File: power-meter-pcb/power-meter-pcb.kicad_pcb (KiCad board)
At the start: 2 copper layers, 0.7 x 0.5 mm, 59 parts, among them J1 Crank interconnect, J2 Debug, J3 USB4120-03-C_REVA, J4 Side A, J5 Side B, Q1 AS2302, Q2 AS2302, Q3 AS2302, SW1 EN, SW2 BOOT, U1 ESP32-S3-WROOM-1, U2 P3T1755, U3 MCP73831-2-OT, U4 TPD3E001DRLR, U5 S-8261AAJMD-G2JT2U, U6 TPS63031DSK, U7 ADS1232IPW

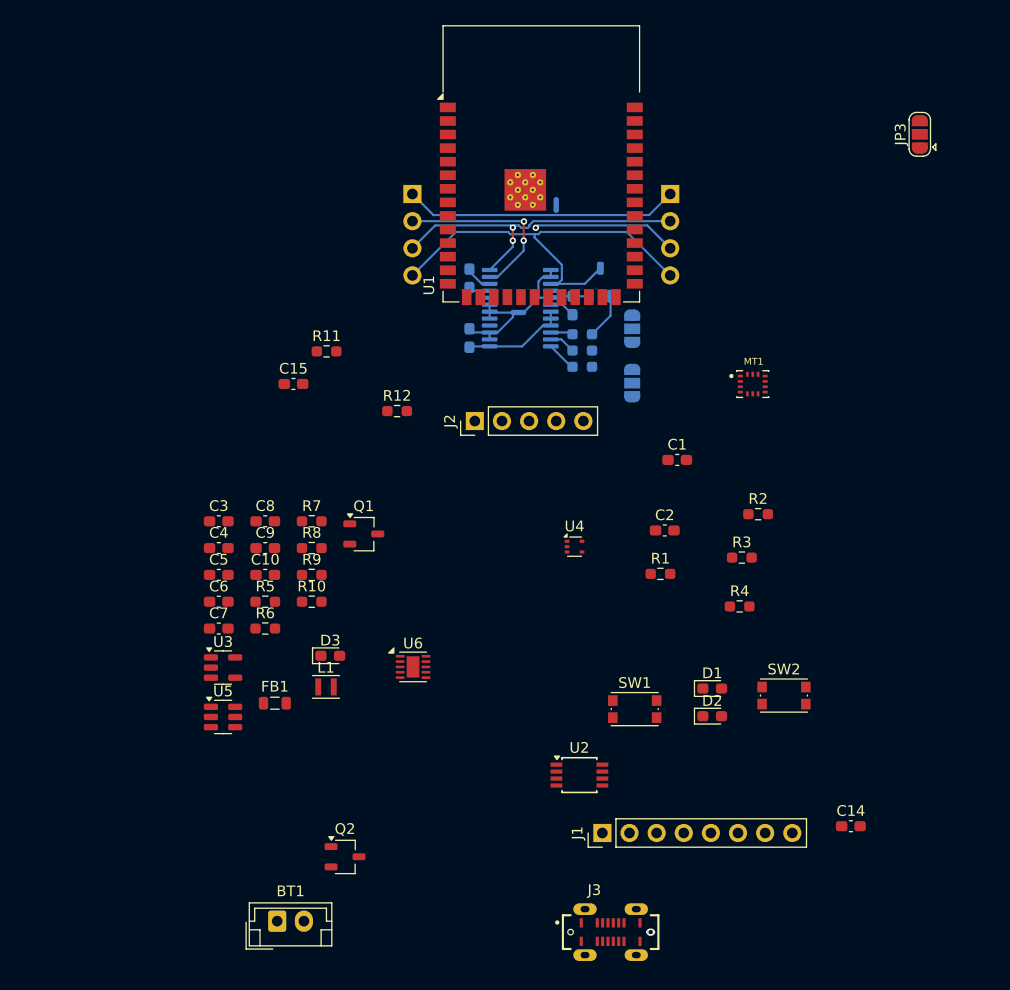
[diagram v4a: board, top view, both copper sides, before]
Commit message: Adding filtering and pullup resistors, board layout
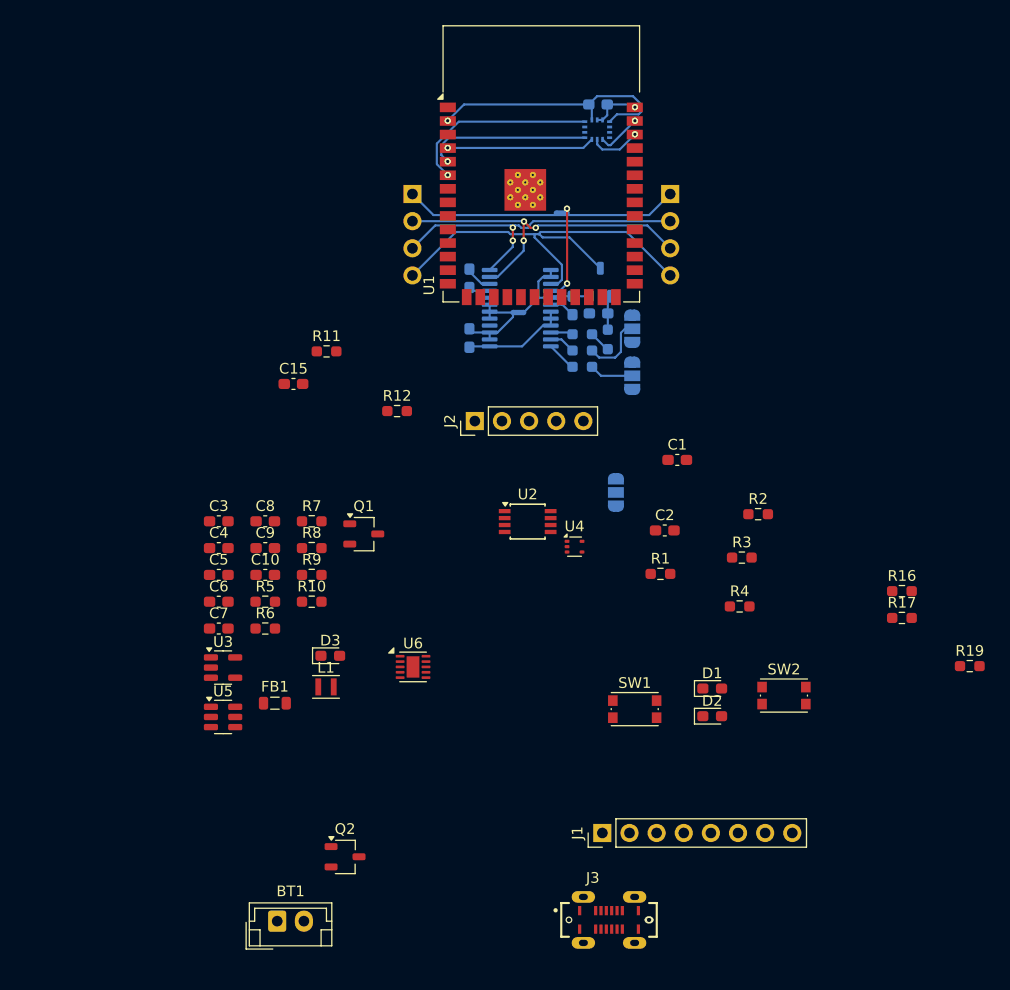
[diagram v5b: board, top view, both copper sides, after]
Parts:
- added C16: 0.1u, Capacitor_SMD:C_0603_1608Metric_Pad1.08x0.95mm_HandSolder, B.Cu at (140.6, 70.1)
- added R16: 4.7k, Resistor_SMD:R_0603_1608Metric_Pad0.98x0.95mm_HandSolder, F.Cu at (169.0, 96.1)
- added R17: 4.7k, Resistor_SMD:R_0603_1608Metric_Pad0.98x0.95mm_HandSolder, F.Cu at (169.0, 98.6)
- added R18: 470, Resistor_SMD:R_0603_1608Metric_Pad0.98x0.95mm_HandSolder, B.Cu at (141.5, 72.5)
- added R19: 47, Resistor_SMD:R_0603_1608Metric_Pad0.98x0.95mm_HandSolder, F.Cu at (175.4, 103.1)
- C14, JP3, MT1: moved to B.Cu
- moved C14 71.6 mm to (140.6, 50.5)
- moved JP3 44.0 mm to (142.2, 86.9)
- moved MT1 27.9 mm to (140.5, 52.9)
- moved U2 24.2 mm to (134.0, 89.6)
- moved J3 1.15 mm to (141.6, 126.9)
- moved NT3 0.91 mm to (137.2, 60.7), turned to 0 degrees
- moved JP1 0.68 mm to (143.8, 75.9)
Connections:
- FB1 pad 1: +3.3V -> Net-(FB1-Pad1)
- J1 pad 6: +BATT -> /Power save
- J1 pad 7: GNDD -> +BATT
- Q3 pad 1: /AMP_PWDN -> Net-(Q3-G)
- U1 pad 15: /Accelerometer/SPI.SDO -> unconnected-(U1-IO3-Pad15)
- U1 pad 23: /USB and charging/Power save -> /Power save
- U1 pad 5: /Accelerometer/Interrupt -> /Accelerometer/SPI.SDO
- U1 pad 6: unconnected-(U1-IO6-Pad6) -> /Accelerometer/Interrupt
- U1 pad 8: unconnected-(U1-IO15-Pad8) -> /I2C.SDA
- U1 pad 9: unconnected-(U1-IO16-Pad9) -> /I2C.SCL
- U6 pad 7: /USB and charging/Power save -> /Power save
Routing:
- net +3.3V: track 9.76 -> 34.8 mm, vias 0 -> 1
- net /Accelerometer/Interrupt: track 0.00 -> 18.1 mm, vias 0 -> 1
- net /Accelerometer/SPI.SDO: track 0.00 -> 15.5 mm, vias 0 -> 1
- net /Accelerometer/SPI.SDI: track 0.00 -> 14.0 mm, vias 0 -> 1
- net /Strain gauge amplifier/GP: track 0.00 -> 8.82 mm, vias 0 -> 2
- net /AMP.SCLK: track 0.00 -> 6.20 mm
- net GNDD: track 10.1 -> 14.9 mm, vias 0 -> 1
- net /Accelerometer/SPI.SCLK: track 0.00 -> 4.80 mm, vias 0 -> 1
- net /Accelerometer/SPI.AC_CS: track 0.00 -> 4.31 mm, vias 0 -> 1
- net /AMP.DOUT: track 0.00 -> 4.11 mm
- net Net-(Q3-G): track 0.00 -> 3.24 mm
- net /AMP_PWDN: track 4.27 -> 2.06 mm
- net /Strain gauge amplifier/GN: track 39.4 -> 41.3 mm
- net /Strain gauge amplifier/GA: track 31.0 -> 32.3 mm

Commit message: Routing and component placement continues
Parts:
- added D4: D, Diode_SMD:D_0603_1608Metric_Pad1.05x0.95mm_HandSolder, B.Cu at (124.7, 80.3)
- C10: renamed from C9; moved to B.Cu
- C11: renamed from C10; moved to B.Cu
- C5: renamed from C6; moved to B.Cu
- C7, C8, D3, FB1, L1, U3, U4, U6: moved to B.Cu
- J1: footprint Connector_PinHeader_2.54mm:PinHeader_1x08_P2.54mm_Vertical -> Connector_JST:JST_PH_B8B-PH-K_1x08_P2.00mm_Vertical
- J4: renamed from BT1; footprint Connector_JST:JST_EH_B2B-EH-A_1x02_P2.50mm_Vertical -> Connector_JST:JST_PH_B2B-PH-K_1x02_P2.00mm_Vertical
- J5: renamed from J4; moved to F.Cu
- J6: renamed from J5; moved to F.Cu
- JP3: moved to F.Cu
- R11: renamed from R9; moved to B.Cu
- R12: renamed from R10; moved to B.Cu
- R15: renamed from R19; moved to B.Cu
- R4: renamed from R16; moved to B.Cu
- R6: renamed from R17; moved to B.Cu
- R8: renamed from R6; moved to B.Cu
- R9: renamed from R7; moved to B.Cu
- moved R6 56.0 mm to (129.4, 58.9), turned to 180 degrees
- moved R4 55.5 mm to (129.4, 57.1), turned to 180 degrees
- moved R15 49.2 mm to (134.5, 75.7), turned to 180 degrees
- moved J4 46.2 mm to (136.4, 88.8)
- moved U5 44.1 mm to (142.9, 84.6), turned to 90 degrees
- moved Q2 42.7 mm to (139.0, 84.5), turned to 180 degrees
- moved D2 40.6 mm to (132.4, 71.9)
- moved J3 40.4 mm to (127.1, 89.2), turned to 180 degrees
- moved C6 39.4 mm to (142.2, 81.7), turned to 180 degrees
- moved FB1 37.2 mm to (131.0, 75.7), turned to 180 degrees
- moved D1 37.0 mm to (132.4, 73.4)
- moved SW2 36.5 mm to (146.1, 71.3)
- moved C7 36.0 mm to (134.0, 78.3)
- moved R12 33.1 mm to (144.5, 84.8), turned to -90 degrees
- moved SW1 32.1 mm to (146.1, 75.1)
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- renumbered C16 to C12, C11 to C13, C12 to C14, C13 to C15, C14 to C16, C5 to C6, C15 to C9, NT3 to NT1, NT1 to NT2, R8 to R10, R12 to R13, R11 to R14, R18 to R16, R13 to R17, R14 to R18, R15 to R19, R4 to R5, R5 to R7
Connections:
- U1 pad 10: unconnected-(U1-IO17-Pad10) -> /USB and charging/Charging
- U1 pad 16: /AMP_PWDN -> unconnected-(U1-IO46-Pad16)
- U1 pad 26: /AMP1.SCLK -> unconnected-(U1-IO45-Pad26)
- U1 pad 33: unconnected-(U1-IO40-Pad33) -> /AMP1.DOUT
- U1 pad 34: unconnected-(U1-IO41-Pad34) -> /AMP1.SCLK
- U1 pad 35: /AMP1.DOUT -> /AMP_PWDN
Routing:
- net +BATT: track 0.00 -> 25.3 mm
- net /I2C.SDA: track 0.00 -> 20.4 mm, vias 0 -> 1
- net GNDD: track 14.9 -> 32.2 mm
- net /I2C.SCL: track 0.00 -> 16.4 mm, vias 0 -> 1
- net +3.3V: track 34.8 -> 48.5 mm, vias 1 -> 2
- net Net-(Q1-G): track 0.00 -> 11.9 mm
- net Net-(J4--): track 0.00 -> 10.5 mm, vias 0 -> 1
- net +5V: track 0.00 -> 7.48 mm
- net Net-(J3-CC1): track 0.00 -> 7.09 mm, vias 0 -> 2
- net Net-(D3-K): track 0.00 -> 6.37 mm
- net Net-(U6-EN): track 0.00 -> 4.73 mm
- net Net-(J3-CC2): track 0.00 -> 3.35 mm
- net Net-(JP3-C): track 0.00 -> 2.37 mm
- net Net-(U6-L1): track 0.00 -> 2.00 mm
- net Net-(U6-L2): track 0.00 -> 1.97 mm
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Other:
- board size 0.7 x 0.5 mm -> 28.7 x 55.6 mm

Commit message: Improved board outline, in the middle of layout changes
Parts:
- added D3: LED, LED_SMD:LED_0603_1608Metric_Pad1.05x0.95mm_HandSolder, F.Cu at (135.9, 75.3)
- added H1: MountingHole, MountingHole:MountingHole_2.2mm_M2, F.Cu at (124.0, 47.0)
- added H2: MountingHole, MountingHole:MountingHole_2.2mm_M2, F.Cu at (146.5, 47.0)
- added H3: MountingHole, MountingHole:MountingHole_2.2mm_M2, F.Cu at (146.5, 95.5)
- added H4: MountingHole, MountingHole:MountingHole_2.2mm_M2, F.Cu at (124.5, 95.5)
- added R7: 150, Resistor_SMD:R_0603_1608Metric_Pad0.98x0.95mm_HandSolder, F.Cu at (135.9, 72.0)
- C6, JP3, Q1, Q2, U2, U5: moved to B.Cu
- J1: footprint Connector_JST:JST_PH_B8B-PH-K_1x08_P2.00mm_Vertical -> Connector_JST:JST_PH_S8B-PH-K_1x08_P2.00mm_Horizontal
- moved C10 38.1 mm to (99.0, 90.4)
- moved C5 38.1 mm to (94.4, 88.5)
- moved D4 38.1 mm to (92.3, 86.8)
- moved D5 38.1 mm to (87.2, 86.8)
- moved R10 38.1 mm to (92.3, 90.3)
- moved R9 38.1 mm to (87.2, 90.3)
- moved U3 38.1 mm to (89.7, 87.8)
- moved U4 38.1 mm to (89.2, 91.0)
- moved C7 38.1 mm to (96.5, 84.8)
- moved C8 38.1 mm to (99.9, 87.9)
- moved L1 38.1 mm to (96.6, 90.9)
- moved U6 38.1 mm to (96.7, 87.8)
- moved C3 37.1 mm to (88.4, 89.9)
- moved R8 37.1 mm to (92.4, 91.7)
- moved C4 37.1 mm to (93.4, 88.9)
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- renumbered D3 to D4, D4 to D5, R9 to R10, R10 to R11, R11 to R12, R12 to R13, R13 to R14, R14 to R15, R15 to R16, R16 to R17, R17 to R18, R18 to R19, R19 to R20, R7 to R8, R8 to R9
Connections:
- net /USB and charging/Battery voltage renamed /USB and power supply/Battery voltage
- net /USB and charging/Charging renamed /USB and power supply/Charging
- J3 pad A6: /USB and charging/USB.DP -> /USB and power supply/USB.D_P
- J3 pad A7: /USB and charging/USB.DN -> /USB and power supply/USB.D_N
- J3 pad B6: /USB and charging/USB.DN -> /USB and power supply/USB.D_N
- J3 pad B7: /USB and charging/USB.DP -> /USB and power supply/USB.D_P
- U1 pad 13: /USB and charging/USB.DN -> /USB and power supply/USB.D_N
- U1 pad 14: /USB and charging/USB.DP -> /USB and power supply/USB.D_P
- U1 pad 20: unconnected-(U1-IO12-Pad20) -> /LED1
- U1 pad 21: unconnected-(U1-IO13-Pad21) -> /LED2
- U1 pad 22: unconnected-(U1-IO14-Pad22) -> /LED3
- U1 pad 26: unconnected-(U1-IO45-Pad26) -> /AMP_PWDN
- U1 pad 31: /LED1 -> /AMP1.DOUT
- U1 pad 32: /LED2 -> /AMP1.SCLK
- U1 pad 33: /AMP1.DOUT -> unconnected-(U1-IO40-Pad33)
- U1 pad 34: /AMP1.SCLK -> unconnected-(U1-IO41-Pad34)
- U1 pad 35: /AMP_PWDN -> unconnected-(U1-IO42-Pad35)
- U4 pad 1: /USB and charging/USB.DP -> /USB and power supply/USB.DP
- U4 pad 2: /USB and charging/USB.DN -> /USB and power supply/USB.DN
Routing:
- net Net-(Q1-G): track 11.9 -> 27.6 mm
- net /AMP2.DOUT: track 0.00 -> 10.9 mm, vias 0 -> 1
- net /I2C.SDA: track 20.4 -> 10.3 mm, vias 1 -> 2
- net +BATT: track 25.3 -> 16.4 mm
- net /BOOT: track 0.00 -> 8.51 mm
- net +3.3V: track 48.5 -> 41.5 mm, vias 2 -> 3
- net /AMP1.DOUT: track 0.00 -> 6.97 mm, vias 0 -> 1
- net /AMP2.SCLK: track 0.00 -> 6.73 mm, vias 0 -> 1
- net /I2C.SCL: track 16.4 -> 9.89 mm
- net Net-(J3-CC1): track 7.09 -> 0.76 mm, vias 2 -> 0
- net /AMP_PWDN: track 2.06 -> 7.38 mm, vias 0 -> 1
- net Net-(J4--): track 10.5 -> 6.19 mm, vias 1 -> 2
- net Net-(U5-VM): track 0.07 -> 3.55 mm, vias 1 -> 0
- net Net-(J3-CC2): track 3.35 -> 0.00 mm
- net Net-(U5-VDD): track 1.86 -> 5.14 mm
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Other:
- board size 28.7 x 55.6 mm -> 29 x 55.5 mm
- board text added: "${REFERENCE}"

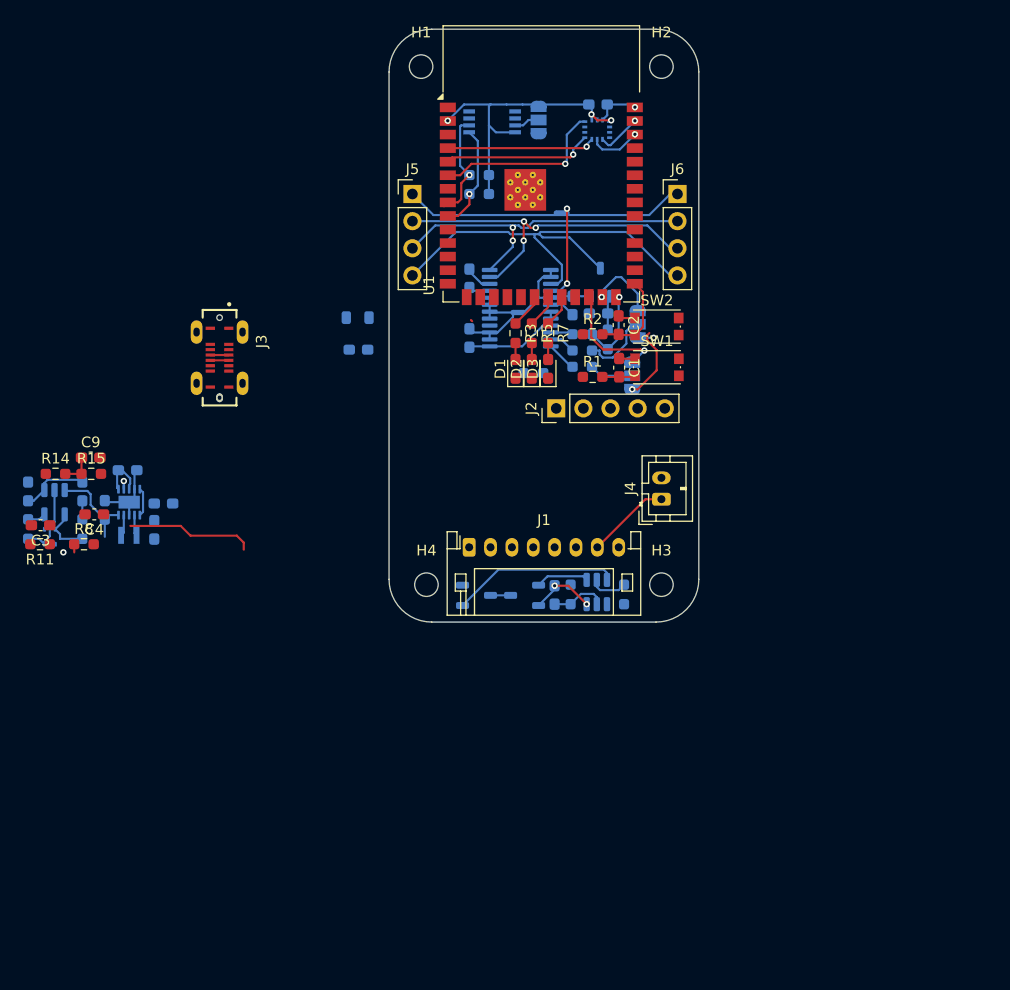
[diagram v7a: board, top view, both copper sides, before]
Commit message: Layout almost done, but will likely swap to a 4 layer PCB
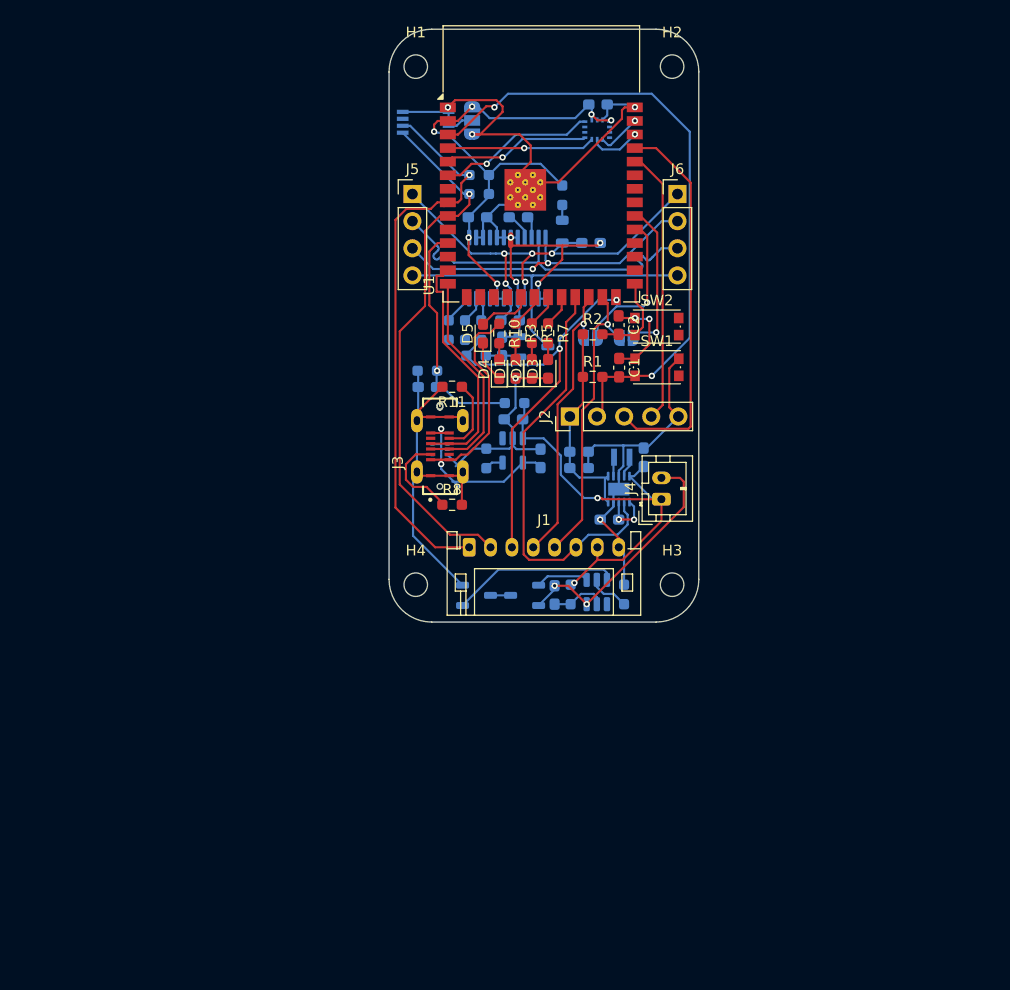
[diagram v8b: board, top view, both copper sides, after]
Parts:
- removed NT1: NetTie_2, NetTie:NetTie-2_SMD_Pad0.5mm
- C3, C4, C9, R14, R15: moved to B.Cu
- D4, D5, NT2, R10: moved to F.Cu
- JP1: value Amp select -> DOUT connect; footprint Jumper:SolderJumper-3_P1.3mm_Open_RoundedPad1.0x1.5mm -> Jumper:SolderJumper-2_P1.3mm_Open_RoundedPad1.0x1.5mm
- JP2: value Amp select -> SCLK connect; footprint Jumper:SolderJumper-3_P1.3mm_Open_RoundedPad1.0x1.5mm -> Jumper:SolderJumper-2_P1.3mm_Open_RoundedPad1.0x1.5mm
- moved C5 50.7 mm to (144.8, 83.6)
- moved C3 47.2 mm to (135.2, 83.7), turned to 90 degrees
- moved L1 46.7 mm to (142.8, 83.6), turned to 0 degrees
- moved U6 45.9 mm to (142.5, 86.6), turned to -90 degrees
- moved C7 45.3 mm to (141.6, 89.4), turned to 180 degrees
- moved D5 45.1 mm to (129.8, 72.0)
- moved R14 43.5 mm to (132.7, 78.5), turned to 180 degrees
- moved R9 43.4 mm to (130.1, 83.7), turned to 90 degrees
- moved U3 43.2 mm to (132.6, 82.9)
- moved R10 43.1 mm to (131.3, 72.0), turned to -90 degrees
- moved R11 41.3 mm to (126.9, 77.0)
- moved D4 40.7 mm to (131.3, 75.3), turned to 90 degrees
- moved C4 40.2 mm to (132.6, 80.0)
- moved C10 40.2 mm to (138.8, 84.6), turned to 0 degrees
- moved C8 39.2 mm to (138.8, 83.1)
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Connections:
- D5 pad 2: /USB and power supply/Charging -> /Charging
- JP1 pad 1: /AMP1.DOUT -> /AMP2.DOUT
- JP1 pad 2: /AMP.DOUT -> /AMP1.DOUT
- JP2 pad 1: /AMP1.SCLK -> /AMP2.SCLK
- JP2 pad 2: /AMP.SCLK -> /AMP1.SCLK
- R18 pad 2: /AMP.DOUT -> /AMP1.DOUT
- R19 pad 2: /AMP.SCLK -> /AMP1.SCLK
- U1 pad 10: /USB and power supply/Charging -> unconnected-(U1-IO17-Pad10)
- U1 pad 19: unconnected-(U1-IO11-Pad19) -> /Charging
- U4 pad 1: /USB and power supply/USB.DP -> /USB and power supply/USB.D_N
- U4 pad 2: /USB and power supply/USB.DN -> /USB and power supply/USB.D_P
- U7 pad 16: /Strain gauge amplifier/GP -> +3.3VA
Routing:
- net GNDD: track 32.3 -> 153.7 mm, vias 1 -> 8
- net /EN: track 3.10 -> 58.7 mm, vias 0 -> 2
- net /I2C.SDA: track 10.3 -> 53.6 mm, vias 2 -> 1
- net /I2C.SCL: track 9.89 -> 50.4 mm
- net /Power save: track 0.76 -> 39.7 mm, vias 1 -> 0
- net /UART.TX: track 0.00 -> 36.2 mm
- net /AMP_PWDN: track 7.38 -> 40.2 mm, vias 1 -> 2
- net +5V: track 4.93 -> 37.7 mm, vias 0 -> 2
- net +3.3V: track 41.5 -> 70.3 mm, vias 3 -> 6
- net /UART.RX: track 0.00 -> 25.7 mm
- net +BATT: track 16.4 -> 39.1 mm, vias 0 -> 2
- net /AMP2.SCLK: track 6.73 -> 27.9 mm
- net /USB and power supply/USB.D_N: track 1.73 -> 22.8 mm
- net /USB and power supply/USB.D_P: track 2.36 -> 21.6 mm
- net /USB and power supply/Battery voltage: track 3.05 -> 22.1 mm, vias 0 -> 1
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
